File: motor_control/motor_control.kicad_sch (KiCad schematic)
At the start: 26 parts, among them J1 GPIO, J10 01x04_GND, J2 MotA, J3 MotB, J4 MOT_POW, J5 UART0, J6 SPI0, J7 I2C1, J8 REG_5V_INPUT, J9 VBUS_OUT, SW1 PU, SW2 PD, SW3 SW_SPDT_312, U1 HC-SR04

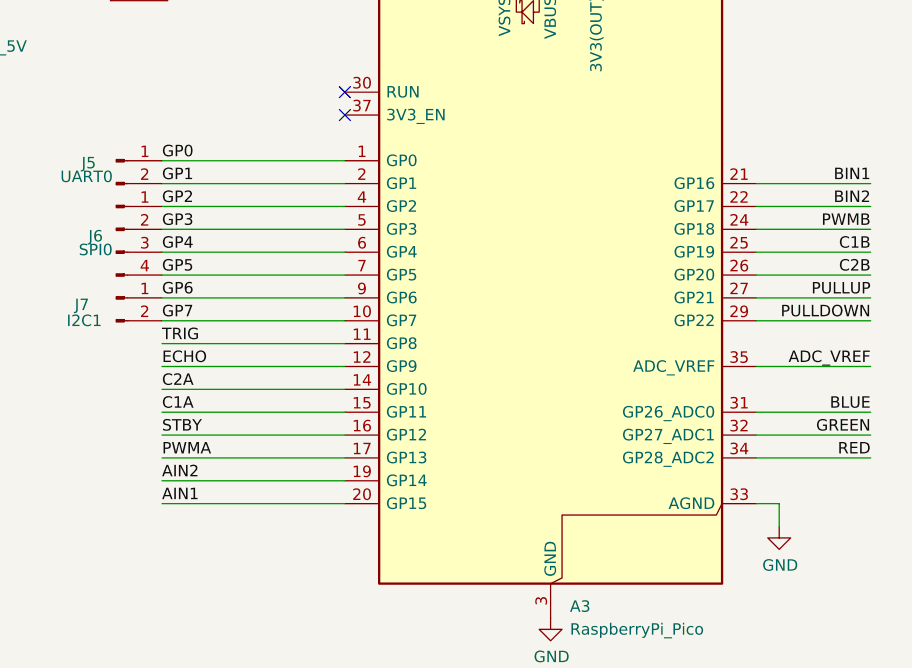
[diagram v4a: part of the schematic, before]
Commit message: relabeling motor control wires
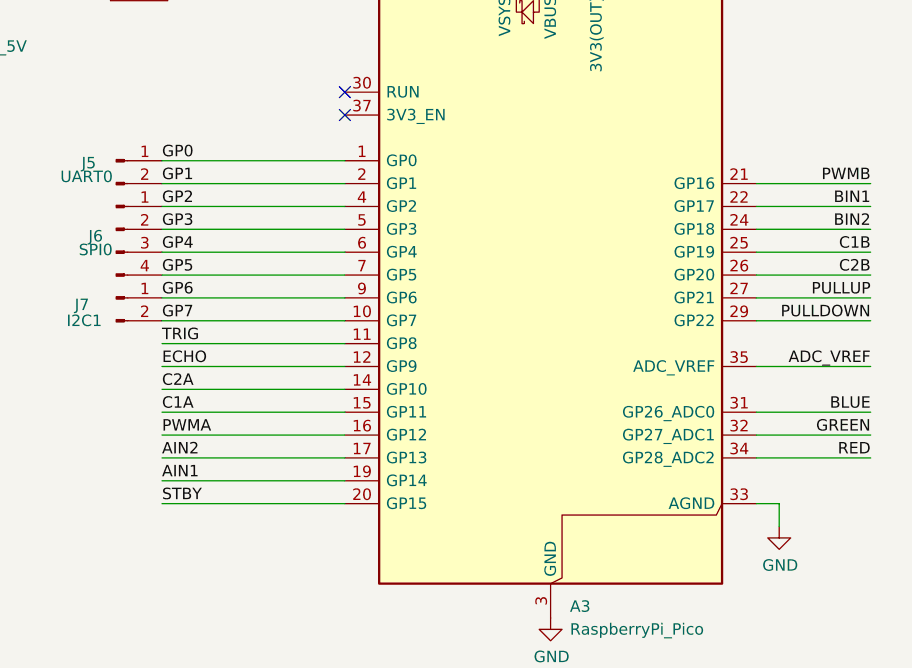
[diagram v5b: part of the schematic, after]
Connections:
- net AIN1: now also A3.19 (GP14); no longer A3.20 (GP15)
- net AIN2: now also A3.17 (GP13); no longer A3.19 (GP14)
- net BIN1: now also A3.22 (GP17); no longer A3.21 (GP16)
- net BIN2: now also A3.24 (GP18); no longer A3.22 (GP17)
- net PWMA: now also A3.16 (GP12); no longer A3.17 (GP13)
- net PWMB: now also A3.21 (GP16); no longer A3.24 (GP18)
- net STBY: now also A3.20 (GP15); no longer A3.16 (GP12)
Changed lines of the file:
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@@
 	)
 	(label "BIN2"
-		(at 264.16 52.07 180)
+		(at 264.16 54.61 180)
 		(effects
 			(font
@@
 	)
 	(label "AIN2"
-		(at 185.42 82.55 0)
+		(at 185.42 80.01 0)
 		(effects
 			(font
@@
 	)
 	(label "STBY"
-		(at 185.42 77.47 0)
+		(at 185.42 85.09 0)
 		(effects
 			(font
@@
 	)
 	(label "BIN1"
-		(at 264.16 49.53 180)
+		(at 264.16 52.07 180)
 		(effects
 			(font
@@
 	)
 	(label "PWMA"
-		(at 185.42 80.01 0)
+		(at 185.42 77.47 0)
 		(effects
 			(font
@@
 	)
 	(label "PWMB"
-		(at 264.16 54.61 180)
+		(at 264.16 49.53 180)
 		(effects
 			(font
@@
 	)
 	(label "AIN1"
-		(at 185.42 85.09 0)
-		(effects
-			(font
+		(at 185.42 82.55 0)
+		(effects
+			(font

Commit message: rearange gp pins
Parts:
- removed J10: 01x04_GND, symbol Connector:Conn_01x04_Pin
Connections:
- net BIN1: now also A3.21 (GP16); no longer A3.22 (GP17)
- net BIN2: now also A3.22 (GP17); no longer A3.24 (GP18)
- net C1B: now also A3.26 (GP20); no longer A3.25 (GP19)
- net C2B: now also A3.25 (GP19); no longer A3.26 (GP20)
- net PWMB: now also A3.24 (GP18); no longer A3.21 (GP16)
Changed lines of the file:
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@@
 	)
 	(junction
-		(at 162.56 95.25)
-		(diameter 0)
-		(color 0 0 0 0)
-	)
-	(junction
 		(at 165.1 148.59)
 		(diameter 0)
@@
 	)
 	(junction
-		(at 162.56 92.71)
-		(diameter 0)
-		(color 0 0 0 0)
-	)
-	(junction
 		(at 58.42 58.42)
 		(diameter 1.016)
@@
 	)
 	(junction
-		(at 162.56 97.79)
-		(diameter 0)
-		(color 0 0 0 0)
-	)
-	(junction
 		(at 165.1 161.29)
 		(diameter 0)
@@
 	(wire
 		(pts
-			(xy 162.56 92.71) (xy 162.56 95.25)
-		)
-		(stroke
-			(width 0)
-			(type default)
-		)
-	)
-	(wire
-		(pts
 			(xy 254 85.09) (xy 254 87.63)
 		)
@@
 	(wire
 		(pts
-			(xy 157.48 90.17) (xy 162.56 90.17)
-		)
-		(stroke
-			(width 0)
-			(type default)
-		)
-	)
-	(wire
-		(pts
 			(xy 195.58 22.86) (xy 187.96 22.86)
 		)
@@
 	(wire
 		(pts
-			(xy 162.56 97.79) (xy 162.56 100.33)
-		)
-		(stroke
-			(width 0)
-			(type default)
-		)
-	)
-	(wire
-		(pts
 			(xy 76.2 50.8) (xy 76.2 63.5)
 		)
@@
 	(wire
 		(pts
-			(xy 157.48 97.79) (xy 162.56 97.79)
-		)
-		(stroke
-			(width 0)
-			(type default)
-		)
-	)
-	(wire
-		(pts
 			(xy 251.46 57.15) (xy 264.16 57.15)
 		)
@@
 	(wire
 		(pts
-			(xy 157.48 95.25) (xy 162.56 95.25)
-		)
-		(stroke
-			(width 0)
-			(type default)
-		)
-	)
-	(wire
-		(pts
 			(xy 60.96 30.48) (xy 31.75 30.48)
 		)
@@
 	(wire
 		(pts
-			(xy 157.48 92.71) (xy 162.56 92.71)
-		)
-		(stroke
-			(width 0)
-			(type default)
-		)
-	)
-	(wire
-		(pts
 			(xy 76.2 24.13) (xy 76.2 27.94)
 		)
@@
 	(wire
 		(pts
-			(xy 162.56 95.25) (xy 162.56 97.79)
-		)
-		(stroke
-			(width 0)
-			(type default)
-		)
-	)
-	(wire
-		(pts
 			(xy 48.26 132.08) (xy 48.26 135.89)
 		)
@@
 	(wire
 		(pts
-			(xy 162.56 90.17) (xy 162.56 92.71)
-		)
-		(stroke
-			(width 0)
-			(type default)
-		)
-	)
-	(wire
-		(pts
 			(xy 168.91 25.4) (xy 177.8 25.4)
 		)
@@
 	)
 	(label "BIN2"
-		(at 264.16 54.61 180)
+		(at 264.16 52.07 180)
 		(effects
 			(font
@@
 	)
 	(label "C1B"
-		(at 264.16 57.15 180)
+		(at 264.16 59.69 180)
 		(effects
 			(font
@@
 	)
 	(label "BIN1"
-		(at 264.16 52.07 180)
+		(at 264.16 49.53 180)
 		(effects
 			(font
@@
 	)
 	(label "PWMB"
-		(at 264.16 49.53 180)
+		(at 264.16 54.61 180)
 		(effects
 			(font
@@
 	)
 	(label "C2B"
-		(at 264.16 59.69 180)
+		(at 264.16 57.15 180)
 		(effects
 			(font
@@
 					(unit 1)
 				)
-			)
-		)
-	)
-	(symbol
-		(lib_id "Connector:Conn_01x04_Pin")
-		(at 152.4 92.71 0)
-		(unit 1)
-		(exclude_from_sim no)
-		(in_bom yes)
-		(on_board yes)
-		(dnp no)
-		(fields_autoplaced yes)
-		(property "Reference" "J10"
-			(at 153.035 85.09 0)
-			(effects
-				(font
-					(size 1.27 1.27)
-				)
-			)
-		)
-		(property "Value" "01x04_GND"
-			(at 153.035 87.63 0)
-			(effects
-				(font
-					(size 1.27 1.27)
-				)
-			)
-		)
-		(property "Footprint" ""
-			(at 152.4 92.71 0)
-			(effects
-				(font
-					(size 1.27 1.27)
-				)
-				(hide yes)
-			)
-		)
-		(property "Datasheet" "~"
-			(at 152.4 92.71 0)
-			(effects
-				(font
-					(size 1.27 1.27)
-				)
-				(hide yes)
-			)
-		)
-		(property "Description" "Generic connector, single row, 01x04, script generated"
-			(at 152.4 92.71 0)
-			(effects
-				(font
-					(size 1.27 1.27)
-				)
-				(hide yes)
-			)
-		)
-		(pin "1"
-		)
-		(pin "4"
-		)
-		(pin "3"
-		)
-		(pin "2"
-		)
-		(instances
-			(project ""
-				(path "/e63e39d7-6ac0-4ffd-8aa3-1841a4541b55"
-					(reference "J10")
-					(unit 1)
-				)
-			)
-		)
-	)
-	(symbol
-		(lib_id "power:GND")
-		(at 162.56 100.33 0)
-		(unit 1)
-		(exclude_from_sim no)
-		(in_bom yes)
-		(on_board yes)
-		(dnp no)
-		(property "Reference" "#PWR032"
-			(at 162.56 106.68 0)
-			(effects
-				(font
-					(size 1.27 1.27)
-				)
-				(hide yes)
-			)
-		)
-		(property "Value" "GND"
-			(at 162.6743 104.6544 0)
-			(effects
-				(font
-					(size 1.27 1.27)
-				)
-			)
-		)
-		(property "Footprint" ""
-			(at 162.56 100.33 0)
-			(effects
-				(font
-					(size 1.27 1.27)
-				)
-			)
-		)
-		(property "Datasheet" ""
-			(at 162.56 100.33 0)
-			(effects
-				(font
-					(size 1.27 1.27)
-				)
-			)
-		)
-		(property "Description" "Power symbol creates a global label with name \"GND\" , ground"
-			(at 162.56 100.33 0)
-			(effects
-				(font
-					(size 1.27 1.27)
-				)
-				(hide yes)
-			)
-		)
-		(pin "1"
-		)
-		(instances
-			(project "motor_control"
-				(path "/e63e39d7-6ac0-4ffd-8aa3-1841a4541b55"
-					(reference "#PWR032")
-					(unit 1)
-				)

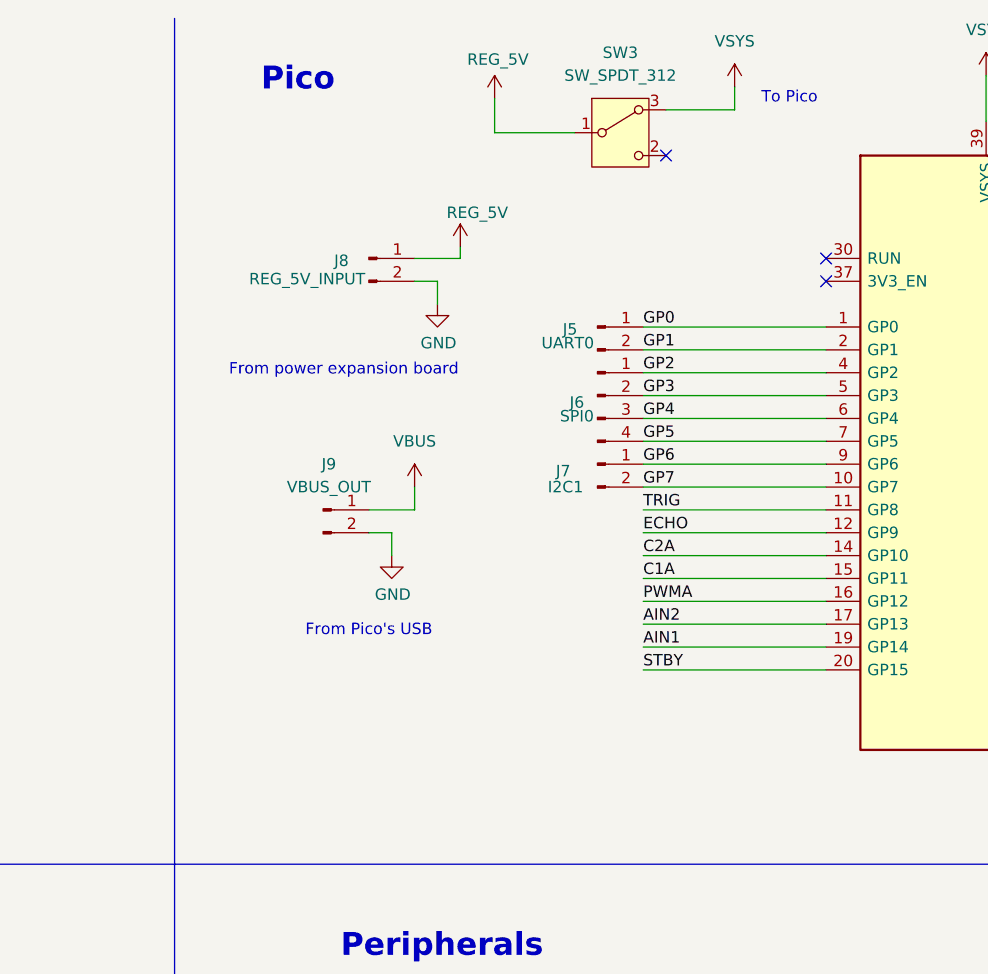
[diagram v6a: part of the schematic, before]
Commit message: rearrange gp0 to gp7 connections
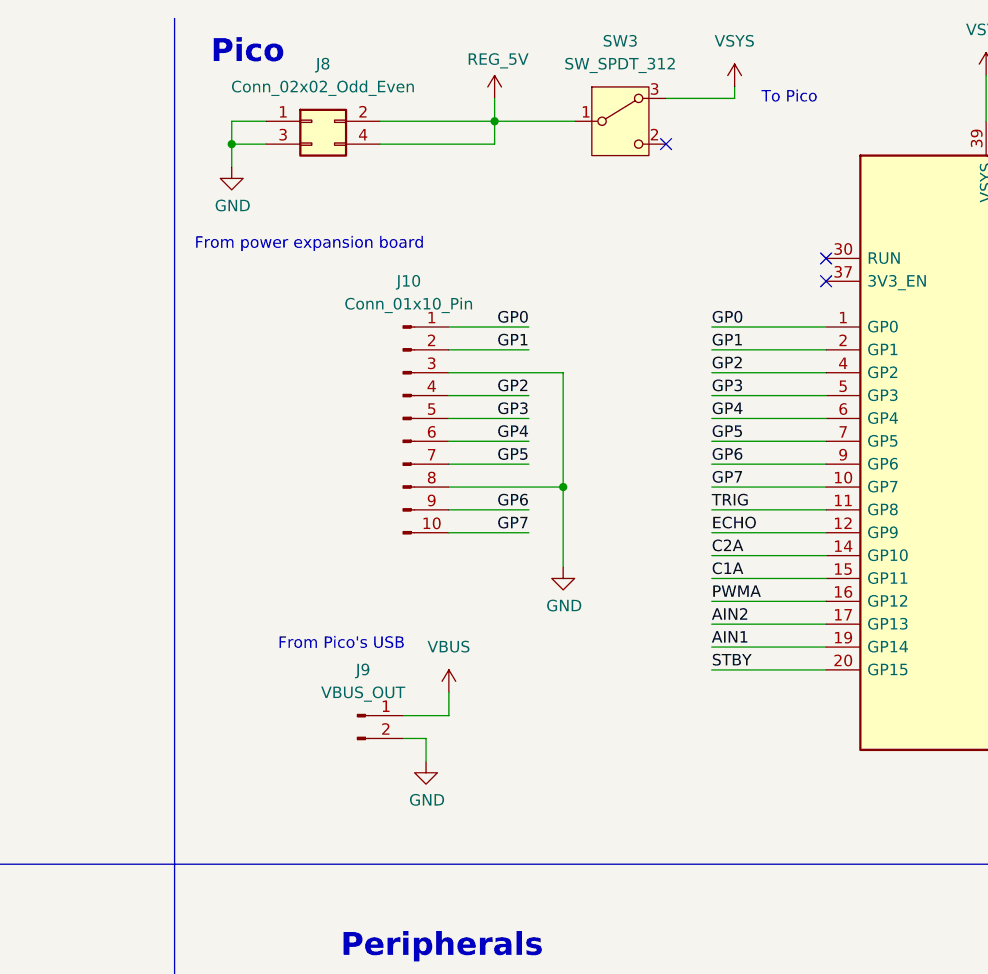
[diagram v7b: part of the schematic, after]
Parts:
- removed J5: UART0, Connector_PinHeader_2.54mm:PinHeader_1x02_P2.54mm_Vertical, symbol Connector:Conn_01x02_Pin
- removed J6: SPI0, Connector_PinHeader_2.54mm:PinHeader_1x04_P2.54mm_Vertical, symbol Connector:Conn_01x04_Pin
- removed J7: I2C1, Connector_PinHeader_2.54mm:PinHeader_1x02_P2.54mm_Vertical, symbol Connector:Conn_01x02_Pin
- removed J8: REG_5V_INPUT, Connector_PinHeader_2.54mm:PinHeader_1x02_P2.54mm_Vertical, symbol Connector:Conn_01x02_Pin
- added J10: Conn_01x10_Pin, symbol Connector:Conn_01x10_Pin
- added J8: Conn_02x02_Odd_Even, symbol Connector_Generic:Conn_02x02_Odd_Even
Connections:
- net GND: now also J10.3 (Pin_3), J10.8 (Pin_8), J8.1 (Pin_1), J8.3 (Pin_3)
- net GP0: now also J10.1 (Pin_1)
- net GP1: now also J10.2 (Pin_2)
- net GP2: now also J10.4 (Pin_4)
- net GP3: now also J10.5 (Pin_5)
- net GP4: now also J10.6 (Pin_6)
- net GP5: now also J10.7 (Pin_7)
- net GP6: now also J10.9 (Pin_9)
- net GP7: now also J10.10 (Pin_10)
- net REG_5V: now also J8.2 (Pin_2), J8.4 (Pin_4)
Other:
- moved on the sheet: J9, SW3

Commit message: assign footprint to connectors
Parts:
- J10: footprint (none) -> Connector_PinHeader_2.54mm:PinHeader_1x10_P2.54mm_Vertical
- J8: footprint (none) -> Connector_PinHeader_2.54mm:PinHeader_2x02_P2.54mm_Vertical
- J9: footprint (none) -> Connector_PinHeader_2.54mm:PinHeader_1x01_P2.54mm_Vertical
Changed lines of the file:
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@@
 			)
 		)
-		(property "Footprint" ""
+		(property "Footprint" "Connector_PinHeader_2.54mm:PinHeader_1x10_P2.54mm_Vertical"
 			(at 158.75 57.15 0)
 			(effects
@@
 			)
 		)
-		(property "Footprint" ""
+		(property "Footprint" "Connector_PinHeader_2.54mm:PinHeader_2x02_P2.54mm_Vertical"
 			(at 148.59 24.13 0)
 			(effects
@@
 			)
 		)
-		(property "Footprint" ""
+		(property "Footprint" "Connector_PinHeader_2.54mm:PinHeader_1x01_P2.54mm_Vertical"
 			(at 153.67 90.17 0)
 			(effects
